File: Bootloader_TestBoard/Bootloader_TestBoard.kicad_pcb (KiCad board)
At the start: 2 copper layers, 86 parts, among them IC1 TCAN3413DR, IC2 TCAN3413DR, J10 SWD, J3 Conn_01x05, J6 Conn_01x03, J7 Conn_01x03, J8 USB_C_Receptacle, J9 SWD, SW1 Reset, U1 MCP1826S, U2 STM32G473VET6, Y1 Crystal, Y2 Crystal

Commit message: boar
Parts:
- removed J10, J9: SWD, Connector_PinHeader_2.54mm:PinHeader_1x04_P2.54mm_Vertical
- removed J7: Conn_01x03, Connector_PinHeader_2.54mm:PinHeader_1x03_P2.54mm_Vertical
- removed J8: USB_C_Receptacle, Project:GCT_USB4105-GF-A
- removed JP5: Jumper, Connector_PinHeader_2.54mm:PinHeader_1x02_P2.54mm_Vertical
- removed R14, R15: 1k, Resistor_SMD:R_0603_1608Metric_Pad0.98x0.95mm_HandSolder
- removed R16, R17: 5.1k, Resistor_SMD:R_0603_1608Metric_Pad0.98x0.95mm_HandSolder
- removed TP3: TestPoint, TestPoint:TestPoint_Loop_D1.80mm_Drill1.0mm_Beaded
- removed kicad-embed://stm32g473cb.pdf1: STM32G473CET6, Project:48PinMCU
- added J1: USB_C_Receptacle, Project:GCT_USB4105-GF-A, F.Cu at (80.6, 121.2)
- added J2: SWD, Connector_PinHeader_2.54mm:PinHeader_1x04_P2.54mm_Vertical, F.Cu at (100.9, 130.6)
- added J4: Conn_01x05, Connector_PinHeader_2.54mm:PinHeader_1x05_P2.54mm_Vertical, F.Cu at (59.3, 121.2)
- added J5: Conn_01x03, Connector_PinHeader_2.54mm:PinHeader_1x03_P2.54mm_Vertical, F.Cu at (69.0, 125.4)
- added JP4: TRM, Connector_PinHeader_2.54mm:PinHeader_1x02_P2.54mm_Vertical, F.Cu at (91.5, 156.0)
- added R10: 60, Resistor_SMD:R_0603_1608Metric_Pad0.98x0.95mm_HandSolder, F.Cu at (98.8, 155.6)
- added R12: 60, Resistor_SMD:R_0603_1608Metric_Pad0.98x0.95mm_HandSolder, F.Cu at (87.6, 153.2)
- added R13: 60, Resistor_SMD:R_0603_1608Metric_Pad0.98x0.95mm_HandSolder, F.Cu at (87.6, 154.8)
- added R9: 10k, Resistor_SMD:R_0603_1608Metric_Pad0.98x0.95mm_HandSolder, F.Cu at (55.7, 148.2)
- added TP2: TestPoint, TestPoint:TestPoint_Loop_D1.80mm_Drill1.0mm_Beaded, F.Cu at (108.0, 121.2)
- added U3: MCP1826S, Package_TO_SOT_SMD:SOT-223-3_TabPin2, F.Cu at (92.8, 124.8)
- C1, C2: value 10u -> 26p; footprint Capacitor_SMD:C_0805_2012Metric_Pad1.18x1.45mm_HandSolder -> Capacitor_SMD:C_0603_1608Metric_Pad1.08x0.95mm_HandSolder
- C10, C5, C6, C8: value 0.1u -> 0.1uF
- C11: value 26p -> 1uF
- C12: value 26p -> 0.1uF
- C14: value 10uF -> 0.1uF; footprint Capacitor_SMD:C_0805_2012Metric -> Capacitor_SMD:C_0603_1608Metric_Pad1.08x0.95mm_HandSolder
- C15: value 0.1uF -> 100nF
- C16, C17: value 0.1uF -> 26p
- C18: value 0.1uF -> 10u; footprint Capacitor_SMD:C_0603_1608Metric_Pad1.08x0.95mm_HandSolder -> Capacitor_SMD:C_0805_2012Metric
- C19, C21: value 1uF -> 0.1u
- C20, C22, C23: value 0.1uF -> 0.1u
- C24: value 0.1uF -> 1u
- C25: value 100nF -> 0.1u
- C26: value 26p -> 1u
- C27: value 26p -> 0.1u
- C28: value 10u -> 0.1u; footprint Capacitor_SMD:C_0805_2012Metric -> Capacitor_SMD:C_0603_1608Metric_Pad1.08x0.95mm_HandSolder
- C3, C7: value 10u -> 0.1uF; footprint Capacitor_SMD:C_0805_2012Metric_Pad1.18x1.45mm_HandSolder -> Capacitor_SMD:C_0603_1608Metric_Pad1.08x0.95mm_HandSolder
- C30, C31, C32: value 0.1u -> 10u; footprint Capacitor_SMD:C_0603_1608Metric_Pad1.08x0.95mm_HandSolder -> Capacitor_SMD:C_0805_2012Metric_Pad1.18x1.45mm_HandSolder
- C34: value 1u -> 0.1u
- C36: value 1u -> 10u; footprint Capacitor_SMD:C_0603_1608Metric_Pad1.08x0.95mm_HandSolder -> Capacitor_SMD:C_0805_2012Metric_Pad1.18x1.45mm_HandSolder
- C4: value 0.1u -> 10uF; footprint Capacitor_SMD:C_0603_1608Metric_Pad1.08x0.95mm_HandSolder -> Capacitor_SMD:C_0805_2012Metric
- C9: value 0.1u -> 1uF
- D1: value SBA130CH-AU_R1_000A1 -> LED; footprint Diode_SMD:D_SOD-323_HandSoldering -> LED_SMD:LED_0603_1608Metric
- D2: value CDSOT23-T24CAN -> D; footprint LHRS_Passives:CDSOT23-T24CAN -> Diode_SMD:D_SOD-123
- D3: value CDSOT23-T24CAN -> TPD2EUSB30DRTR; footprint LHRS_Passives:CDSOT23-T24CAN -> Project:DRT0003A
- D4: value RGB_LED -> LED; footprint Project:RGB_LED -> LED_SMD:LED_0603_1608Metric
- D5: value LED -> RGB_LED; footprint LED_SMD:LED_0603_1608Metric -> Project:RGB_LED
- D6: value LED -> SBA130CH-AU_R1_000A1; footprint LED_SMD:LED_0603_1608Metric -> Diode_SMD:D_SOD-323_HandSoldering
- D7: value D -> CDSOT23-T24CAN; footprint Diode_SMD:D_SOD-123 -> LHRS_Passives:CDSOT23-T24CAN
- D8: value TPD2EUSB30DRTR -> CDSOT23-T24CAN; footprint Project:DRT0003A -> LHRS_Passives:CDSOT23-T24CAN
- J3: value Conn_01x05 -> SWD; footprint Connector_PinHeader_2.54mm:PinHeader_1x05_P2.54mm_Vertical -> Connector_PinHeader_2.54mm:PinHeader_1x04_P2.54mm_Vertical
- JP1, JP2: value TRM -> Jumper
- JP3: value Jumper -> TRM
- R1, R4: value 60 -> 1k
- R11: value 10k -> 60
- R2, R3: value 60 -> 5.1k
- R5: value 10k -> 1k
- R8: value 1k -> 10k
- U1: value MCP1826S -> STM32G473CET6; footprint Package_TO_SOT_SMD:SOT-223-3_TabPin2 -> Project:48PinMCU
- moved FB3 132.6 mm to (56.8, 154.5), turned to -90 degrees
- moved R5 126.9 mm to (49.1, 149.7), turned to 180 degrees
- moved C26 126.0 mm to (59.8, 154.5), turned to 90 degrees
- moved FB4 122.6 mm to (67.9, 154.2), turned to 180 degrees
- moved C24 121.8 mm to (62.8, 154.5), turned to 90 degrees
- moved C19 120.6 mm to (58.3, 154.5), turned to 90 degrees
- moved C20 120.5 mm to (54.8, 150.7), turned to 180 degrees
- moved D4 120.0 mm to (50.0, 155.0)
- moved C29 119.2 mm to (64.4, 154.5), turned to 90 degrees
- moved C22 116.9 mm to (51.2, 139.0)
- moved C27 116.5 mm to (71.3, 154.5), turned to -90 degrees
- moved C21 115.5 mm to (61.3, 154.5), turned to 90 degrees
- moved C39 115.2 mm to (87.6, 156.4)
- moved C16 114.2 mm to (51.0, 142.2)
- moved C17 113.8 mm to (51.0, 143.7)
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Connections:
- C1 pad 2: Net-(D1-K) -> Net-(U1-PF0-OSC_IN)
- C10 pad 1: GND -> +3V3_48P
- C10 pad 2: Net-(C10-Pad2) -> GND
- C11 pad 1: GND -> /48Pin/VDDA
- C11 pad 2: Net-(kicad-embed://stm32g473cb.pdf1-PF0-OSC_IN) -> /48Pin/GNDA
- C12 pad 1: Net-(kicad-embed://stm32g473cb.pdf1-PF1-OSC_OUT) -> +3V3_48P
- C13 pad 1: /48Pin/VDDA -> +3V3_48P
- C13 pad 2: /48Pin/GNDA -> GND
- C15 pad 1: /48Pin/NRST -> /48Pin/VDDA
- C15 pad 2: GND -> /48Pin/GNDA
- C16 pad 1: +3V3_48P -> GND
- C16 pad 2: GND -> Net-(U2-PF0-OSC_IN)
- C17 pad 1: /48Pin/VDDA -> GND
- C17 pad 2: /48Pin/GNDA -> Net-(U2-PF1-OSC_OUT)
- C18 pad 1: +3V3_48P -> +3V3_100P
- C19 pad 1: /48Pin/VDDA -> /100Pin/VDDA
- C19 pad 2: /48Pin/GNDA -> /100Pin/GNDA
- C2 pad 1: GND -> Net-(U1-PF1-OSC_OUT)
- C2 pad 2: +3V3 -> GND
- C20 pad 1: +3V3_48P -> +3V3_100P
- C21 pad 1: /48Pin/VDDA -> /100Pin/VDDA
- C21 pad 2: /48Pin/GNDA -> /100Pin/GNDA
- C22 pad 1: +3V3_48P -> /100Pin/NRST
- C23 pad 1: +3V3_48P -> +3V3_100P
- C24 pad 1: +3V3_48P -> /100Pin/VDDA
- C24 pad 2: GND -> /100Pin/GNDA
- C25 pad 1: /48Pin/VDDA -> +3V3_100P
- C25 pad 2: /48Pin/GNDA -> GND
- C26 pad 1: GND -> /100Pin/VDDA
- C26 pad 2: Net-(U2-PF0-OSC_IN) -> /100Pin/GNDA
- C27 pad 1: GND -> +3V3_100P
- C27 pad 2: Net-(U2-PF1-OSC_OUT) -> GND
- C3 pad 1: +3V3_48P -> /48Pin/VDDA
- C3 pad 2: GND -> /48Pin/GNDA
- C30 pad 1: +3V3_100P -> GND
- C30 pad 2: GND -> Net-(D6-K)
- C31 pad 1: /100Pin/VDDA -> GND
- C31 pad 2: /100Pin/GNDA -> +3V3
- C32 pad 1: /100Pin/NRST -> +3V3_48P
- C33 pad 1: +3V3_100P -> +3V3_48P
- C34 pad 1: /100Pin/VDDA -> +3V3_48P
- C34 pad 2: /100Pin/GNDA -> GND
- C35 pad 1: +3V3_100P -> GND
- C35 pad 2: GND -> Net-(C35-Pad2)
- C36 pad 1: /100Pin/VDDA -> +3V3_100P
- C36 pad 2: /100Pin/GNDA -> GND
- C39 pad 1: /100Pin/VDDA -> GND
- C39 pad 2: /100Pin/GNDA -> Net-(C39-Pad2)
- C5 pad 1: +3V3_48P -> /48Pin/NRST
- C6 pad 1: GND -> +3V3_48P
- C6 pad 2: Net-(C6-Pad2) -> GND
- C7 pad 1: +3V3_100P -> /48Pin/VDDA
- C7 pad 2: GND -> /48Pin/GNDA
- C8 pad 1: +3V3_100P -> +3V3_48P
- C9 pad 1: +3V3_100P -> /48Pin/VDDA
- C9 pad 2: GND -> /48Pin/GNDA
- D1 pad 1: Net-(D1-K) -> GND
- D1 pad 2: +5V -> Net-(D1-A)
- D2 pad 1: /CAN1/CAN_H -> +5V
- D2 pad 2: /CAN1/CAN_L -> Net-(D2-A)
- D3 pad 1: /CAN2/CAN_H -> /USB_DM
- D3 pad 2: /CAN2/CAN_L -> /USB_DP
- D4 pad 1: /GPIO_B -> GND
- D4 pad 2: Net-(D4-Pad2) -> Net-(D4-A)
- D5 pad 1: GND -> /GPIO_B
- D5 pad 2: Net-(D5-A) -> Net-(D5-Pad2)
- D6 pad 1: GND -> Net-(D6-K)
- D6 pad 2: Net-(D6-A) -> +5V
- D7 pad 1: +5V -> /CAN_H
- D7 pad 2: Net-(D7-A) -> /CAN_L
- D8 pad 1: /USB_DM -> /CAN_H
- D8 pad 2: /USB_DP -> /CAN_L
- IC1 pad 6: /CAN1/CAN_L -> /CAN_L
- IC1 pad 7: /CAN1/CAN_H -> /CAN_H
- IC2 pad 6: /CAN2/CAN_L -> /CAN_L
- IC2 pad 7: /CAN2/CAN_H -> /CAN_H
- J3 pad 1: /USB_DM -> +3V3_100P
- J3 pad 2: /USB_DP -> /SWCLK_100P
- J3 pad 3: /CAN_L -> /SWDIO_100P
- J3 pad 4: /CAN_H -> GND
- J6 pad 1: /USB_DM_48P -> /USB_DP_48P
- J6 pad 2: /USB_DM -> /USB_DP
- J6 pad 3: /USB_DM_100P -> /USB_DP_100P
- JP1 pad 1: Net-(JP1-A) -> +3V3
- JP1 pad 2: /CAN1/CAN_L -> +3V3_100P
- JP2 pad 1: Net-(JP2-A) -> +3V3
- JP2 pad 2: /CAN2/CAN_L -> +3V3_48P
- JP3 pad 1: +3V3 -> Net-(JP3-A)
- JP3 pad 2: +3V3_100P -> /CAN_L
- R1 pad 1: /CAN1/CAN_H -> /48Pin/PA3
- R1 pad 2: Net-(C6-Pad2) -> Net-(D1-A)
- R11 pad 1: /100Pin/NRST -> Net-(C35-Pad2)
- R11 pad 2: +3V3_100P -> Net-(JP3-A)
- R2 pad 1: Net-(C6-Pad2) -> Net-(J1-CC1)
- R2 pad 2: Net-(JP1-A) -> GND
- R3 pad 1: /CAN2/CAN_H -> Net-(J1-CC2)
- R3 pad 2: Net-(C10-Pad2) -> GND
- R4 pad 1: Net-(C10-Pad2) -> /100Pin/PA3
- R4 pad 2: Net-(JP2-A) -> Net-(D4-A)
- R5 pad 1: /48Pin/NRST -> Net-(D5-Pad2)
- R5 pad 2: +3V3_48P -> GND
- R6 pad 1: Net-(D4-Pad2) -> Net-(D5-Pad4)
- R7 pad 1: Net-(D4-Pad4) -> Net-(D5-Pad6)
- R8 pad 1: Net-(D4-Pad6) -> /48Pin/NRST
- R8 pad 2: GND -> +3V3_48P
- U1 pad 1: Net-(D1-K) -> +3V3_48P
- U1 pad 2: GND -> /48Pin/PC13
- U1 pad 3: +3V3 -> /48Pin/PC14
- Y1 pad 1: Net-(kicad-embed://stm32g473cb.pdf1-PF0-OSC_IN) -> Net-(U1-PF0-OSC_IN)
- Y1 pad 2: Net-(kicad-embed://stm32g473cb.pdf1-PF1-OSC_OUT) -> Net-(U1-PF1-OSC_OUT)
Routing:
- net +3V3_100P: track 0.00 -> 92.1 mm, vias 0 -> 4
- net /CAN_H: track 0.00 -> 85.7 mm, vias 0 -> 1
- net +3V3_48P: track 0.00 -> 82.8 mm
- net /CAN_L: track 0.00 -> 76.5 mm, vias 0 -> 1
- net /GPIO_B: track 0.00 -> 71.3 mm, vias 0 -> 3
- net /GPIO_R: track 0.00 -> 66.0 mm, vias 0 -> 2
- net /GPIO_G: track 0.00 -> 63.6 mm, vias 0 -> 3
- net +3V3: track 0.00 -> 58.2 mm
- net /USB_DM_48P: track 0.00 -> 45.1 mm, vias 0 -> 1
- net /USB_DM: track 0.00 -> 36.0 mm, vias 0 -> 1
- net /USB_DP: track 0.00 -> 35.8 mm, vias 0 -> 1
- net /USB_DP_48P: track 0.00 -> 31.1 mm, vias 0 -> 1
- net /SWDIO_48P: track 0.00 -> 28.9 mm, vias 0 -> 1
- net /SWCLK_48P: track 0.00 -> 25.0 mm, vias 0 -> 1
- net GND: track 0.00 -> 24.5 mm, vias 0 -> 70
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- added copper zone on B.Cu, net GND
- added copper zone on F.Cu, net GND
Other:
- board outline added: 63.5 x 39.5 mm
- board text added: "100P"
- board text added: "100P Power"
- board text added: "100P Reset"
- board text added: "3V3"
- board text added: "48P"
- board text added: "48P Power"
- board text added: "48P Reset"
- board text added: "CAN Termination"
- board text added: "CAN_H"
- board text added: "CAN_L"
- board text added: "CLK"
- board text added: "Debug LED"
- board text added: "GND"
- board text added: "IO"
- board text added: "USB+"
- board text added: "USB-"
- board text added: "bootldr test board"

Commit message: changes
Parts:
- removed J4: Conn_01x05, Connector_PinHeader_2.54mm:PinHeader_1x05_P2.54mm_Vertical
- removed J5, J6: Conn_01x03, Connector_PinHeader_2.54mm:PinHeader_1x03_P2.54mm_Vertical
- removed JP1, JP2: Jumper, Connector_PinHeader_2.54mm:PinHeader_1x02_P2.54mm_Vertical
- removed TP1: TestPoint, TestPoint:TestPoint_Loop_D1.80mm_Drill1.0mm_Beaded
- added +3V3: 3.3V, TestPoint:TestPoint_Loop_D1.80mm_Drill1.0mm_Beaded, F.Cu at (58.5, 121.2)
- added C40: 10u, Capacitor_SMD:C_0805_2012Metric_Pad1.18x1.45mm_HandSolder, F.Cu at (72.5, 123.5)
- added C41: 10u, Capacitor_SMD:C_0805_2012Metric_Pad1.18x1.45mm_HandSolder, F.Cu at (75.2, 135.9)
- added D10: D, Diode_SMD:D_SOD-123, F.Cu at (69.2, 128.2)
- added D11: TPD2EUSB30DRTR, Project:USB_TVS, F.Cu at (65.2, 127.8)
- added D12: SBA130CH-AU_R1_000A1, Diode_SMD:D_SOD-323_HandSoldering, F.Cu at (73.2, 126.5)
- added D9: RGB_LED, LHRS_Special:RGB_LED, F.Cu at (103.8, 142.3)
- added G***: LOGO, LOGO, F.Cu at (96.2, 130.7)
- added G***: LOGO, LOGO, F.Cu at (64.6, 131.6)
- added J7: USB_C_Receptacle, Project:USB_Conn, F.Cu at (65.9, 120.3)
- added J8: Conn_01x03, Connector_PinHeader_2.54mm:PinHeader_1x03_P2.54mm_Vertical, F.Cu at (49.5, 121.5)
- added R14: 1k, Resistor_SMD:R_0603_1608Metric_Pad0.98x0.95mm_HandSolder, F.Cu at (107.1, 140.5)
- added R15: 1k, Resistor_SMD:R_0603_1608Metric_Pad0.98x0.95mm_HandSolder, F.Cu at (107.1, 142.0)
- added R16: 1k, Resistor_SMD:R_0603_1608Metric_Pad0.98x0.95mm_HandSolder, F.Cu at (107.1, 143.5)
- added R17: 5.1k, Resistor_SMD:R_0603_1608Metric_Pad0.98x0.95mm_HandSolder, F.Cu at (67.2, 127.8)
- added R18: 5.1k, Resistor_SMD:R_0603_1608Metric_Pad0.98x0.95mm_HandSolder, F.Cu at (62.8, 126.8)
- added U4: MCP1826S, Package_TO_SOT_SMD:SOT-223-3_TabPin2, F.Cu at (75.0, 131.2)
- C19, C21, C24, C26, C29, FB3: moved to B.Cu
- D3: footprint Project:DRT0003A -> Project:USB_TVS
- D5: footprint Project:RGB_LED -> LHRS_Special:RGB_LED
- J1: footprint Project:GCT_USB4105-GF-A -> Project:USB_Conn
- Reset1, SW1: footprint Project:TL3365AF180QG -> LHRS_Special:TL3365AF180QG
- U1: footprint Project:48PinMCU -> LHRS_Special:48PinMCU
- U2: footprint Project:100PinMCU -> LHRS_Special:100PinMCU
- moved FB3 12.2 mm to (69.0, 154.6), turned to 90 degrees
- moved R9 9.48 mm to (53.4, 139.0), turned to 0 degrees
- moved C19 9.19 mm to (67.5, 154.6), turned to -90 degrees
- moved C25 6.50 mm to (56.0, 136.5)
- moved R8 6.24 mm to (103.5, 139.5), turned to 180 degrees
- moved C26 6.19 mm to (66.0, 154.6), turned to -90 degrees
- moved C21 3.19 mm to (64.5, 154.6), turned to -90 degrees
- moved C29 2.99 mm to (61.4, 154.6), turned to -90 degrees
- moved +3V3 2.80 mm to (101.0, 121.2)
- moved R3 2.44 mm to (78.2, 126.7), turned to 180 degrees
- moved D5 2.08 mm to (54.5, 148.0)
- moved R7 1.49 mm to (50.4, 147.3)
- moved R6 1.44 mm to (50.4, 148.8)
- moved C1 1.41 mm to (106.5, 150.1), turned to 90 degrees
- moved R5 1.40 mm to (50.4, 150.3)
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- renumbered TP_3.3V1 to +3V3, TP2 to GND
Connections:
- net +5V renamed +5V_48P
- +3V3 pad 1: +3V3 -> +3V3_48P
- C31 pad 2: +3V3 -> +3V3_48P
- D3 pad 1: /USB_DM -> /USB_DM_48P
- D3 pad 2: /USB_DP -> /USB_DP_48P
- D5 pad 1: /GPIO_B -> /100Pin/PA2
- D5 pad 3: /GPIO_R -> /100Pin/PA1
- D5 pad 5: /GPIO_G -> /100Pin/PA0
- J1 pad A6: /USB_DP -> /USB_DP_48P
- J1 pad A7: /USB_DM -> /USB_DM_48P
- J1 pad B6: /USB_DP -> /USB_DP_48P
- J1 pad B7: /USB_DM -> /USB_DM_48P
- U1 pad 10: /GPIO_G -> /48Pin/PA2
- U1 pad 8: /GPIO_B -> /48Pin/PA0
- U1 pad 9: /GPIO_R -> /48Pin/PA1
- U2 pad 20: /GPIO_B -> /100Pin/PA0
- U2 pad 21: /GPIO_R -> /100Pin/PA1
- U2 pad 22: /GPIO_G -> /100Pin/PA2
- U3 pad 3: +3V3 -> +3V3_48P
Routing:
- net /GPIO_B: track 71.3 -> 0.00 mm, vias 3 -> 0
- net /GPIO_R: track 66.0 -> 0.00 mm, vias 2 -> 0
- net /GPIO_G: track 63.6 -> 0.00 mm, vias 3 -> 0
- net +3V3: track 58.2 -> 0.00 mm
- net /USB_DM: track 36.0 -> 0.00 mm, vias 1 -> 0
- net /USB_DP: track 35.8 -> 0.00 mm, vias 1 -> 0
- net +3V3_48P: track 82.8 -> 109.0 mm
- net +5V_48P: track 21.5 -> 2.74 mm
- net /USB_DM_48P: track 45.1 -> 29.5 mm, vias 1 -> 2
- net +3V3_100P: track 92.1 -> 105.6 mm
- net GND: track 24.5 -> 35.5 mm, vias 70 -> 57
- net Net-(D10-A): track 0.00 -> 8.95 mm
- net /USB_DP_100P: track 14.2 -> 21.6 mm, vias 1 -> 2
- net Net-(D12-K): track 0.00 -> 6.74 mm
- net +5V_100P: track 0.00 -> 4.54 mm
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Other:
- board text added: "48->"
- board text added: "<-100"
- board text removed: "100P Power"
- board text removed: "48P Power"
- board text removed: "USB+"
- board text removed: "USB-"

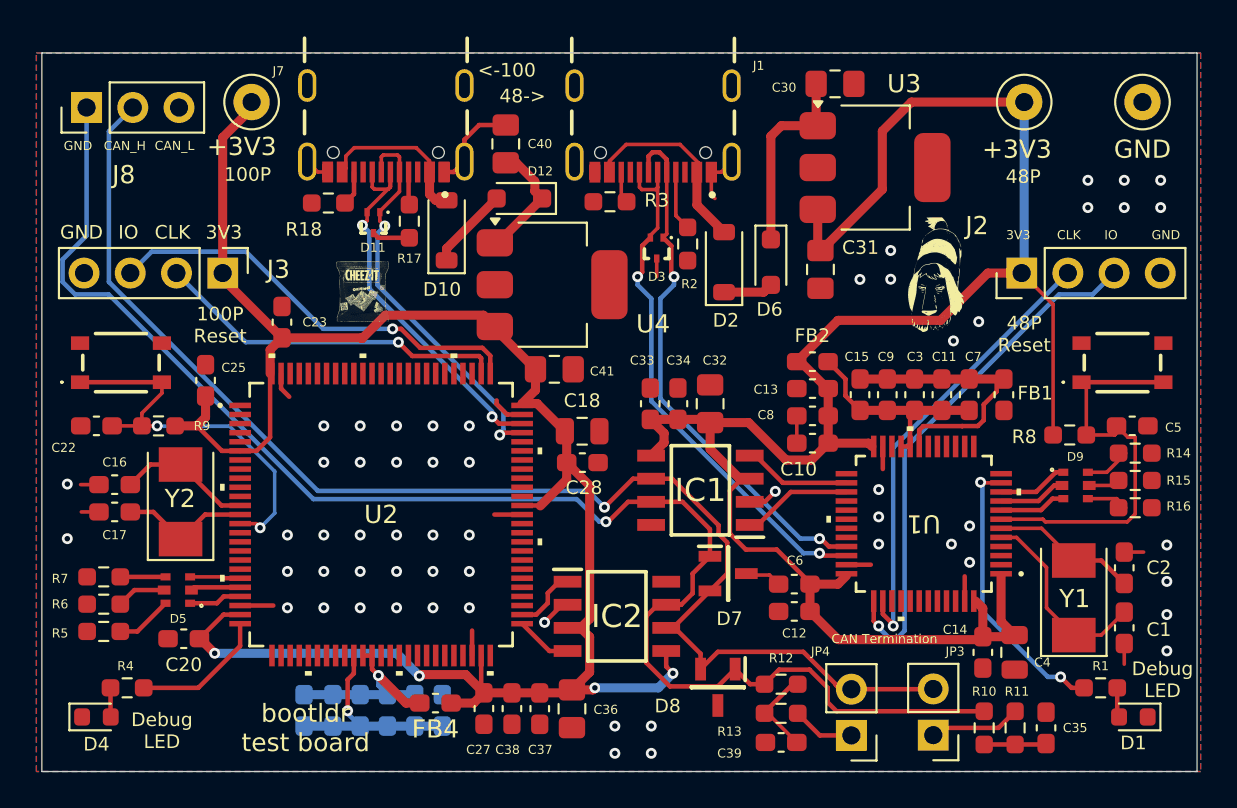
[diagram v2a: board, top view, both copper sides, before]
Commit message: better keepout ; round edges ; name
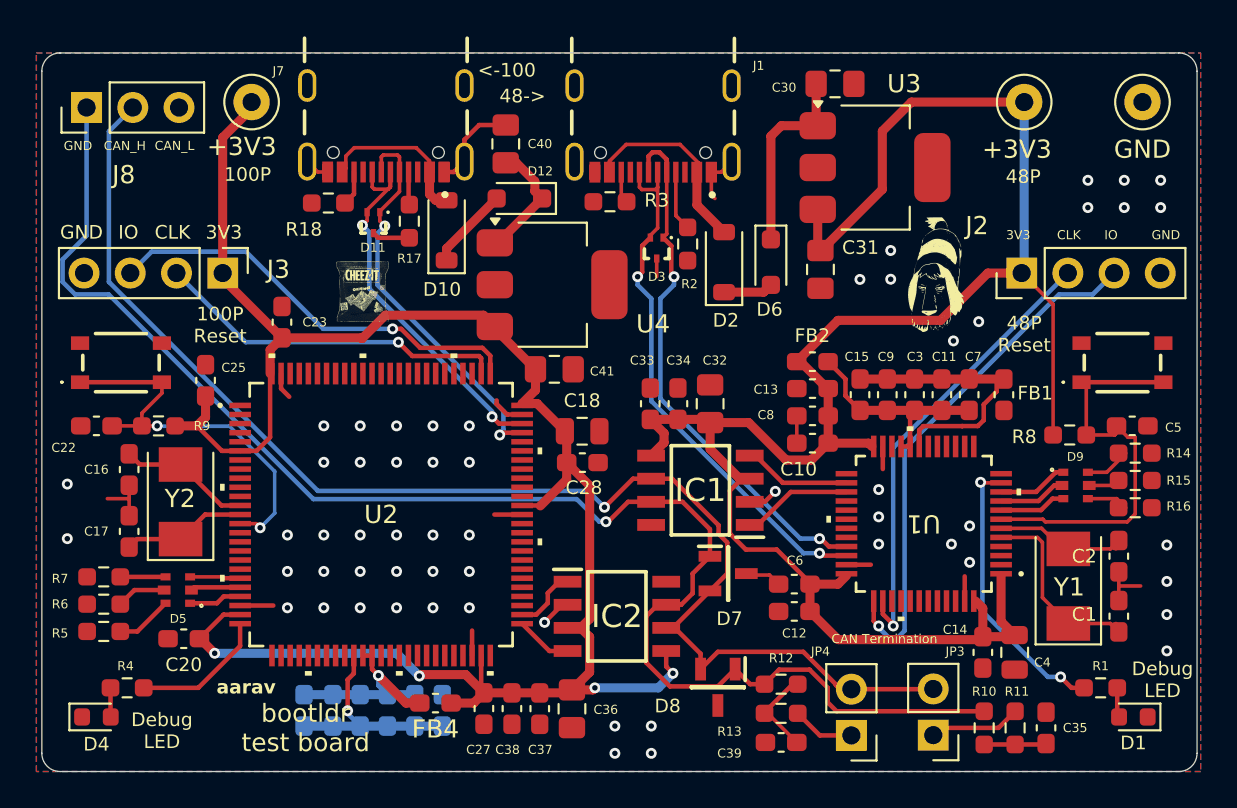
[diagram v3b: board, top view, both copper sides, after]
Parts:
- moved C17 1.33 mm to (51.8, 144.8), turned to -90 degrees
- moved C16 1.15 mm to (51.8, 141.4), turned to 90 degrees
- moved C2 0.70 mm to (106.2, 146.2), turned to -90 degrees
- moved C1 0.70 mm to (106.2, 149.5), turned to -90 degrees
- moved Y1 0.70 mm to (103.4, 147.8)
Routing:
- net GND: track 35.5 -> 37.1 mm
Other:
- outline, holes or cut-outs redrawn
- board text added: "aarav"
